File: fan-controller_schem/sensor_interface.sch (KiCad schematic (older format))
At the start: 11 parts, among them Q601 BC556

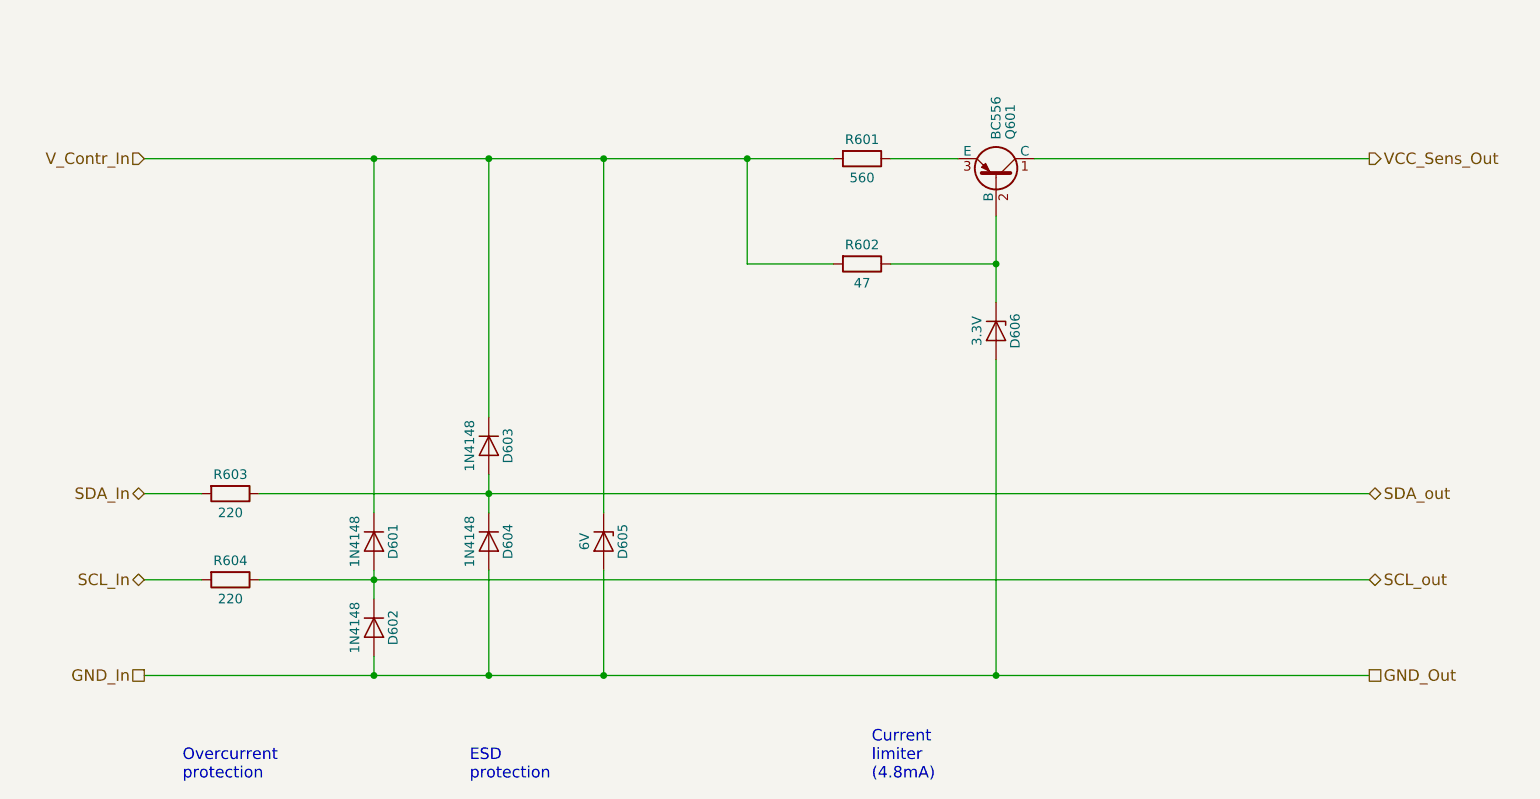
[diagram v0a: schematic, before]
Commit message: Experimentation phase. Investigations re. frequency characteristics of the TL071 OPAMP.
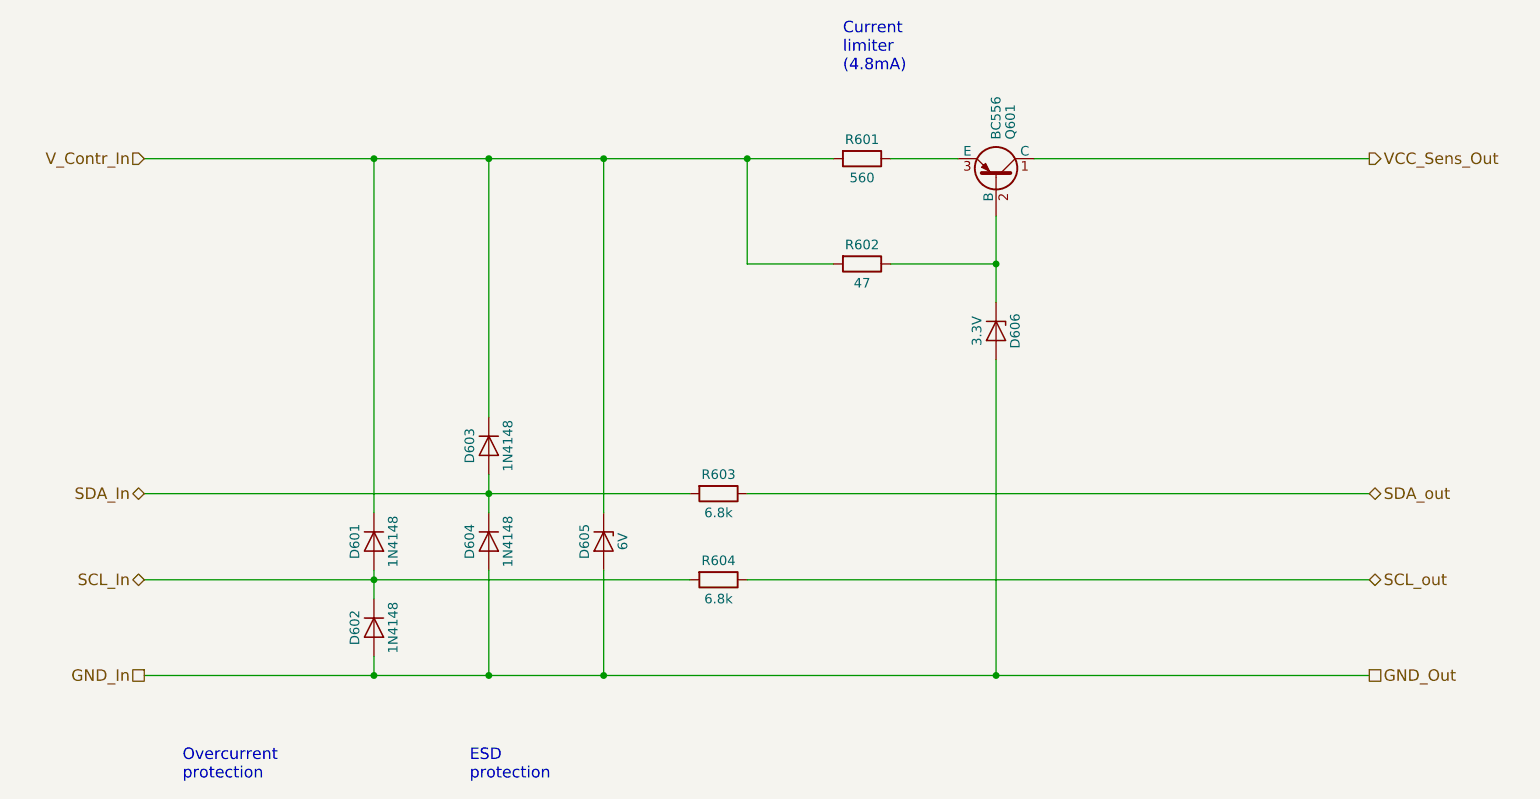
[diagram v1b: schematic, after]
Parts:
- R603, R604: value 220 -> 6.8k
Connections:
- net SCL_In: now also D601.2 (A), D602.1 (K)
- net SCL_out: no longer D601.2 (A), D602.1 (K)
- net SDA_In: now also D603.2 (A), D604.1 (K)
- net SDA_out: no longer D603.2 (A), D604.1 (K)
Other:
- moved on the sheet: R603, R604
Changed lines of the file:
@@
 U 1 1 58F34910
 P 3300 4800
-F 0 "D602" H 3300 4900 50  0000 C CNN
-F 1 "1N4148" H 3300 4700 50  0000 C CNN
+F 0 "D602" H 3300 4700 50  0000 C CNN
+F 1 "1N4148" H 3300 4900 50  0000 C CNN
 F 2 "" H 3300 4800 50  0001 C CNN
 F 3 "" H 3300 4800 50  0001 C CNN
@@
 U 1 1 58F34A47
 P 3300 4350
-F 0 "D601" H 3300 4450 50  0000 C CNN
-F 1 "1N4148" H 3300 4250 50  0000 C CNN
+F 0 "D601" H 3300 4250 50  0000 C CNN
+F 1 "1N4148" H 3300 4450 50  0000 C CNN
 F 2 "" H 3300 4350 50  0001 C CNN
 F 3 "" H 3300 4350 50  0001 C CNN
@@
 U 1 1 58F34C65
 P 3900 3850
-F 0 "D603" H 3900 3950 50  0000 C CNN
-F 1 "1N4148" H 3900 3750 50  0000 C CNN
+F 0 "D603" H 3900 3750 50  0000 C CNN
+F 1 "1N4148" H 3900 3950 50  0000 C CNN
 F 2 "" H 3900 3850 50  0001 C CNN
 F 3 "" H 3900 3850 50  0001 C CNN
@@
 U 1 1 58F34DBA
 P 3900 4350
-F 0 "D604" H 3900 4450 50  0000 C CNN
-F 1 "1N4148" H 3900 4250 50  0000 C CNN
+F 0 "D604" H 3900 4250 50  0000 C CNN
+F 1 "1N4148" H 3900 4450 50  0000 C CNN
 F 2 "" H 3900 4350 50  0001 C CNN
 F 3 "" H 3900 4350 50  0001 C CNN
@@
 U 1 1 58F34DFA
 P 4500 4350
-F 0 "D605" H 4500 4450 50  0000 C CNN
-F 1 "6V" H 4500 4250 50  0000 C CNN
+F 0 "D605" H 4500 4250 50  0000 C CNN
+F 1 "6V" H 4500 4450 50  0000 C CNN
 F 2 "" H 4500 4350 50  0001 C CNN
 F 3 "" H 4500 4350 50  0001 C CNN
@@
 $EndComp
 Wire Wire Line
-	2100 2350 3300 2350
+	2100 2350 5700 2350
 Wire Wire Line
-	3300 2350 3900 2350
-Wire Wire Line
-	3900 2350 4500 2350
-Wire Wire Line
-	4500 2350 5250 2350
-Wire Wire Line
-	5250 2350 5700 2350
-Wire Wire Line
-	2100 5050 3300 5050
-Wire Wire Line
-	3300 5050 3900 5050
-Wire Wire Line
-	3900 5050 4500 5050
-Wire Wire Line
-	4500 5050 6550 5050
-Wire Wire Line
-	6550 5050 8500 5050
+	2100 5050 8500 5050
 Connection ~ 3300 5050
 Wire Wire Line
@@
 Connection ~ 4500 5050
 Wire Wire Line
-	6550 2650 6550 2900
-Wire Wire Line
-	6550 2900 6550 3100
+	6550 2650 6550 3100
 Wire Wire Line
 	6550 5050 6550 3400
@@
 Connection ~ 3900 2350
 Wire Wire Line
-	3900 4000 3900 4100
-Wire Wire Line
-	3900 4100 3900 4200
+	3900 4000 3900 4200
 Wire Wire Line
 	3900 5050 3900 4500
@@
 	3300 5050 3300 4950
 Wire Wire Line
-	3300 4500 3300 4550
-Wire Wire Line
-	3300 4550 3300 4650
+	3300 4500 3300 4650
 Wire Wire Line
 	3300 4200 3300 2350
 Connection ~ 3300 2350
 Wire Wire Line
-	2700 4550 3300 4550
+	2100 4550 4950 4550
 Wire Wire Line
-	3300 4550 8500 4550
+	5250 4550 8500 4550
 Connection ~ 3300 4550
 Wire Wire Line
-	2700 4100 3900 4100
+	2100 4100 4950 4100
 Wire Wire Line
-	3900 4100 8500 4100
+	5250 4100 8500 4100
 Connection ~ 3900 4100
 Text HLabel 8500 5050 2    60   UnSpc ~ 0
@@
 L R R603
 U 1 1 58F3853B
-P 2550 4100
-F 0 "R603" V 2450 4100 50  0000 C CNN
-F 1 "220" V 2650 4100 50  0000 C CNN
-F 2 "" V 2480 4100 50  0001 C CNN
-F 3 "" H 2550 4100 50  0001 C CNN
-	1    2550 4100
+P 5100 4100
+F 0 "R603" V 5000 4100 50  0000 C CNN
+F 1 "6.8k" V 5200 4100 50  0000 C CNN
+F 2 "" V 5030 4100 50  0001 C CNN
+F 3 "" H 5100 4100 50  0001 C CNN
+	1    5100 4100
 	0    1    1    0
 $EndComp
@@
 L R R604
 U 1 1 58F386CB
-P 2550 4550
-F 0 "R604" V 2450 4550 50  0000 C CNN
-F 1 "220" V 2650 4550 50  0000 C CNN
-F 2 "" V 2480 4550 50  0001 C CNN
-F 3 "" H 2550 4550 50  0001 C CNN
-	1    2550 4550
+P 5100 4550
+F 0 "R604" V 5000 4550 50  0000 C CNN
+F 1 "6.8k" V 5200 4550 50  0000 C CNN
+F 2 "" V 5030 4550 50  0001 C CNN
+F 3 "" H 5100 4550 50  0001 C CNN
+	1    5100 4550
 	0    1    1    0
 $EndComp
-Wire Wire Line
-	2100 4100 2400 4100
-Wire Wire Line
-	2100 4550 2400 4550
 Text Notes 2300 5600 0    60   ~ 0
 Overcurrent\nprotection
 Text Notes 3800 5600 0    60   ~ 0
 ESD\nprotection
-Text Notes 5900 5600 0    60   ~ 0
+Text Notes 5750 1900 0    60   ~ 0
 Current\nlimiter\n(4.8mA)
 $EndSCHEMATC
